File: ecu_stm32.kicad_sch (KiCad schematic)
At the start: 46 parts, among them J17 ARM Cortex Debug, Y2 16MHz

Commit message: Lots of routing
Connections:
- net +3.3V: now also R104.2
- net +3V3: no longer R104.2
- net IMU_INT1: now also U40.151 (PD7); no longer U40.152 (PG9)
- net IMU_INT2: now also U40.152 (PG9); no longer U40.151 (PD7)
- net RADIO1_DIO0: now also U40.19 (PF3); no longer U40.18 (PF2)
- net RADIO1_DIO1: now also U40.18 (PF2); no longer U40.19 (PF3)
- net RADIO2_DIO0: now also U40.12 (PI10); no longer U40.11 (PI9)
- net RADIO2_DIO1: now also U40.11 (PI9); no longer U40.12 (PI10)
- net RADIO_DIO0: now also U40.17 (PF1); no longer U40.16 (PF0)
- net RADIO_DIO1: now also U40.16 (PF0); no longer U40.17 (PF1)
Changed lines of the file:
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@@
 	(global_label "RADIO1_DIO1"
 		(shape input)
-		(at 193.04 76.2 0)
+		(at 193.04 73.66 0)
 		(fields_autoplaced yes)
 		(effects
@@
 		)
 		(property "Intersheetrefs" "${INTERSHEET_REFS}"
-			(at 208.181 76.2 0)
+			(at 208.181 73.66 0)
 			(effects
 				(font
@@
 	(global_label "RADIO2_DIO1"
 		(shape input)
-		(at 256.54 114.3 0)
+		(at 256.54 111.76 0)
 		(fields_autoplaced yes)
 		(effects
@@
 		)
 		(property "Intersheetrefs" "${INTERSHEET_REFS}"
-			(at 271.681 114.3 0)
+			(at 271.681 111.76 0)
 			(effects
 				(font
@@
 	(global_label "IMU_INT2"
 		(shape input)
-		(at 256.54 38.1 0)
+		(at 226.06 91.44 180)
 		(fields_autoplaced yes)
 		(effects
@@
 				(size 1.27 1.27)
 			)
-			(justify left)
+			(justify right)
 		)
 		(property "Intersheetrefs" "${INTERSHEET_REFS}"
-			(at 267.9919 38.1 0)
+			(at 214.6081 91.44 0)
 			(effects
 				(font
 					(size 1.27 1.27)
 				)
-				(justify left)
+				(justify right)
 				(hide yes)
 			)
@@
 	(global_label "RADIO_DIO0"
 		(shape input)
-		(at 193.04 68.58 0)
+		(at 193.04 71.12 0)
 		(fields_autoplaced yes)
 		(effects
@@
 		)
 		(property "Intersheetrefs" "${INTERSHEET_REFS}"
-			(at 206.9715 68.58 0)
+			(at 206.9715 71.12 0)
 			(effects
 				(font
@@
 	(global_label "RADIO2_DIO0"
 		(shape input)
-		(at 256.54 111.76 0)
+		(at 256.54 114.3 0)
 		(fields_autoplaced yes)
 		(effects
@@
 		)
 		(property "Intersheetrefs" "${INTERSHEET_REFS}"
-			(at 271.681 111.76 0)
+			(at 271.681 114.3 0)
 			(effects
 				(font
@@
 	(global_label "RADIO1_DIO0"
 		(shape input)
-		(at 193.04 73.66 0)
+		(at 193.04 76.2 0)
 		(fields_autoplaced yes)
 		(effects
@@
 		)
 		(property "Intersheetrefs" "${INTERSHEET_REFS}"
-			(at 208.181 73.66 0)
+			(at 208.181 76.2 0)
 			(effects
 				(font
@@
 	(global_label "IMU_INT1"
 		(shape input)
-		(at 226.06 91.44 180)
+		(at 256.54 38.1 0)
 		(fields_autoplaced yes)
 		(effects
@@
 				(size 1.27 1.27)
 			)
-			(justify right)
+			(justify left)
 		)
 		(property "Intersheetrefs" "${INTERSHEET_REFS}"
-			(at 214.6875 91.44 0)
+			(at 267.9919 38.1 0)
 			(effects
 				(font
 					(size 1.27 1.27)
 				)
-				(justify right)
+				(justify left)
 				(hide yes)
 			)
@@
 	(global_label "RADIO_DIO1"
 		(shape input)
-		(at 193.04 71.12 0)
+		(at 193.04 68.58 0)
 		(fields_autoplaced yes)
 		(effects
@@
 		)
 		(property "Intersheetrefs" "${INTERSHEET_REFS}"
-			(at 206.9715 71.12 0)
+			(at 206.9715 68.58 0)
 			(effects
 				(font
@@
 	)
 	(symbol
+		(lib_id "power:+3.3V")
+		(at 69.85 67.31 270)
+		(unit 1)
+		(exclude_from_sim no)
+		(in_bom yes)
+		(on_board yes)
+		(dnp no)
+		(property "Reference" "#PWR0228"
+			(at 66.04 67.31 0)
+			(effects
+				(font
+					(size 1.27 1.27)
+				)
+				(hide yes)
+			)
+		)
+		(property "Value" "+3.3V"
+			(at 73.66 67.31 0)
+			(effects
+				(font
+					(size 1.27 1.27)
+				)
+			)
+		)
+		(property "Footprint" ""
+			(at 69.85 67.31 0)
+			(effects
+				(font
+					(size 1.27 1.27)
+				)
+				(hide yes)
+			)
+		)
+		(property "Datasheet" ""
+			(at 69.85 67.31 0)
+			(effects
+				(font
+					(size 1.27 1.27)
+				)
+				(hide yes)
+			)
+		)
+		(property "Description" ""
+			(at 69.85 67.31 0)
+			(effects
+				(font
+					(size 1.27 1.27)
+				)
+				(hide yes)
+			)
+		)
+		(pin "1"
+		)
+		(instances
+			(project "rocket2-ecu"
+				(path "/02606b2c-b376-4ffb-9781-f9cea3f70994/d71af74c-6b83-4356-8066-aa44d85885b6"
+					(reference "#PWR0228")
+					(unit 1)
+				)
+			)
+		)
+	)
+	(symbol
 		(lib_id "Device:C_Small")
 		(at 80.01 129.54 90)
@@
 					(unit 1)
 				)
-			)
-		)
-	)
-	(symbol
-		(lib_id "power:+3V3")
-		(at 69.85 67.31 270)
-		(unit 1)
-		(exclude_from_sim no)
-		(in_bom yes)
-		(on_board yes)
-		(dnp no)
-		(property "Reference" "#PWR0228"
-			(at 66.04 67.31 0)
-			(effects
-				(font
-					(size 1.27 1.27)
-				)
-				(hide yes)
-			)
-		)
-		(property "Value" "+3V3"
-			(at 75.438 67.31 90)
-			(effects
-				(font
-					(size 1.27 1.27)
-				)
-			)
-		)
-		(property "Footprint" ""
-			(at 69.85 67.31 0)
-			(effects
-				(font
-					(size 1.27 1.27)
-				)
-				(hide yes)
-			)
-		)
-		(property "Datasheet" ""
-			(at 69.85 67.31 0)
-			(effects
-				(font
-					(size 1.27 1.27)
-				)
-				(hide yes)
-			)
-		)
-		(property "Description" ""
-			(at 69.85 67.31 0)
-			(effects
-				(font
-					(size 1.27 1.27)
-				)
-				(hide yes)
-			)
-		)
-		(pin "1"
-		)
-		(instances
-			(project "rocket2-ecu"
-				(path "/02606b2c-b376-4ffb-9781-f9cea3f70994/d71af74c-6b83-4356-8066-aa44d85885b6"
-					(reference "#PWR0228")
-					(unit 1)
-				)

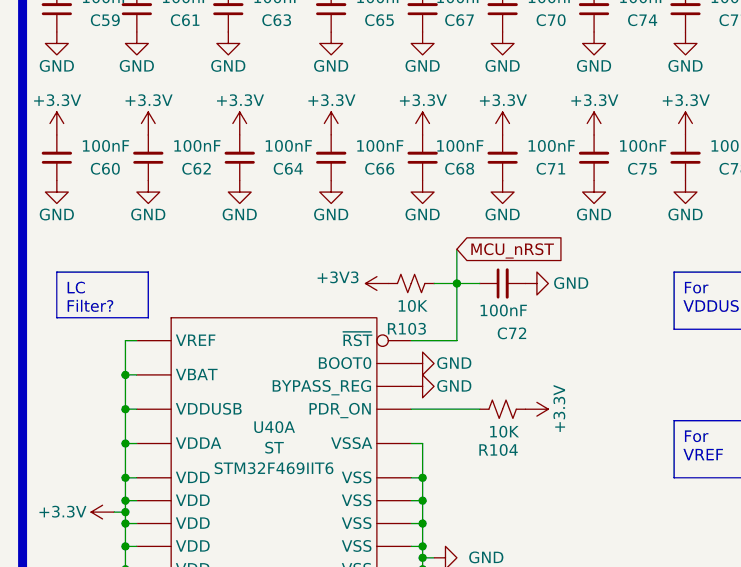
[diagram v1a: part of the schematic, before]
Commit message: More routing, only GPS and REDS radio left
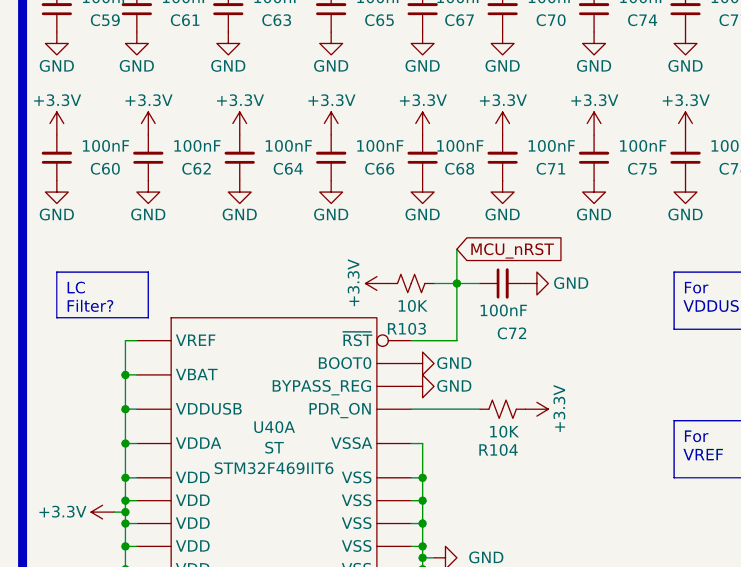
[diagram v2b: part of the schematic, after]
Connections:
- net +3V3 is gone; now on net +3.3V: R103.1
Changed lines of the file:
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@@
+	)
+	(symbol
+		(lib_id "power:+3.3V")
+		(at 54.61 53.34 90)
+		(unit 1)
+		(exclude_from_sim no)
+		(in_bom yes)
+		(on_board yes)
+		(dnp no)
+		(property "Reference" "#PWR075"
+			(at 58.42 53.34 0)
+			(effects
+				(font
+					(size 1.27 1.27)
+				)
+				(hide yes)
+			)
+		)
+		(property "Value" "+3.3V"
+			(at 50.8 53.34 0)
+			(effects
+				(font
+					(size 1.27 1.27)
+				)
+			)
+		)
+		(property "Footprint" ""
+			(at 54.61 53.34 0)
+			(effects
+				(font
+					(size 1.27 1.27)
+				)
+				(hide yes)
+			)
+		)
+		(property "Datasheet" ""
+			(at 54.61 53.34 0)
+			(effects
+				(font
+					(size 1.27 1.27)
+				)
+				(hide yes)
+			)
+		)
+		(property "Description" ""
+			(at 54.61 53.34 0)
+			(effects
+				(font
+					(size 1.27 1.27)
+				)
+				(hide yes)
+			)
+		)
+		(pin "1"
+		)
+		(instances
+			(project "rocket2-ecu"
+				(path "/02606b2c-b376-4ffb-9781-f9cea3f70994/d71af74c-6b83-4356-8066-aa44d85885b6"
+					(reference "#PWR075")
+					(unit 1)
+				)
+			)
+		)
 	)
 	(symbol
@@
 					(unit 1)
 				)
-			)
-		)
-	)
-	(symbol
-		(lib_id "power:+3V3")
-		(at 54.61 53.34 90)
-		(unit 1)
-		(exclude_from_sim no)
-		(in_bom yes)
-		(on_board yes)
-		(dnp no)
-		(fields_autoplaced yes)
-		(property "Reference" "#PWR0214"
-			(at 58.42 53.34 0)
-			(effects
-				(font
-					(size 1.27 1.27)
-				)
-				(hide yes)
-			)
-		)
-		(property "Value" "+3V3"
-			(at 51.435 52.705 90)
-			(effects
-				(font
-					(size 1.27 1.27)
-				)
-				(justify left)
-			)
-		)
-		(property "Footprint" ""
-			(at 54.61 53.34 0)
-			(effects
-				(font
-					(size 1.27 1.27)
-				)
-				(hide yes)
-			)
-		)
-		(property "Datasheet" ""
-			(at 54.61 53.34 0)
-			(effects
-				(font
-					(size 1.27 1.27)
-				)
-				(hide yes)
-			)
-		)
-		(property "Description" ""
-			(at 54.61 53.34 0)
-			(effects
-				(font
-					(size 1.27 1.27)
-				)
-				(hide yes)
-			)
-		)
-		(pin "1"
-		)
-		(instances
-			(project "rocket2-ecu"
-				(path "/02606b2c-b376-4ffb-9781-f9cea3f70994/d71af74c-6b83-4356-8066-aa44d85885b6"
-					(reference "#PWR0214")
-					(unit 1)
-				)

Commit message: Updated with Daniels suggestions
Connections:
- net ETH_RX: now also U40.79 (PB10); no longer U40.80 (PB11)
- net ETH_TX: now also U40.80 (PB11); no longer U40.79 (PB10)
- net GPS_RX: now also U40.40 (PA0); no longer U40.41 (PA1)
- net GPS_TX: now also U40.41 (PA1); no longer U40.40 (PA0)
- net GPS_SCL: no longer names the net of U40.45 (PH4)
- net GPS_SDA: no longer names the net of U40.46 (PH5)
- no-connect marks 71 -> 73
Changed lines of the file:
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@@
 	)
 	(no_connect
+		(at 256.54 78.74)
+	)
+	(no_connect
+		(at 256.54 81.28)
+	)
+	(no_connect
 		(at 256.54 40.64)
 	)
@@
 	(global_label "GPS_RX"
 		(shape input)
-		(at 162.56 22.86 180)
+		(at 162.56 20.32 180)
 		(fields_autoplaced yes)
 		(effects
@@
 		)
 		(property "Intersheetrefs" "${INTERSHEET_REFS}"
-			(at 152.3782 22.86 0)
+			(at 152.3782 20.32 0)
 			(effects
 				(font
@@
 		)
 	)
-	(global_label "GPS_SCL"
-		(shape input)
-		(at 256.54 78.74 0)
-		(fields_autoplaced yes)
-		(effects
-			(font
-				(size 1.27 1.27)
-			)
-			(justify left)
-		)
-		(property "Intersheetrefs" "${INTERSHEET_REFS}"
-			(at 267.6705 78.74 0)
-			(effects
-				(font
-					(size 1.27 1.27)
-				)
-				(justify left)
-				(hide yes)
-			)
-		)
-	)
 	(global_label "MCU_nRST"
 		(shape input)
@@
 	(global_label "ETH_TX"
 		(shape input)
-		(at 193.04 45.72 0)
-		(fields_autoplaced yes)
-		(effects
-			(font
-				(size 1.27 1.27)
-			)
-			(justify left)
-		)
-		(property "Intersheetrefs" "${INTERSHEET_REFS}"
-			(at 202.5376 45.72 0)
-			(effects
-				(font
-					(size 1.27 1.27)
-				)
-				(justify left)
-				(hide yes)
-			)
-		)
-	)
-	(global_label "GPS_SDA"
-		(shape input)
-		(at 256.54 81.28 0)
+		(at 193.04 48.26 0)
 		(fields_autoplaced yes)
 		(effects
@@
 		)
 		(property "Intersheetrefs" "${INTERSHEET_REFS}"
-			(at 267.731 81.28 0)
+			(at 202.5376 48.26 0)
 			(effects
 				(font
@@
 	(global_label "ETH_RX"
 		(shape input)
-		(at 193.04 48.26 0)
+		(at 193.04 45.72 0)
 		(fields_autoplaced yes)
 		(effects
@@
 		)
 		(property "Intersheetrefs" "${INTERSHEET_REFS}"
-			(at 202.84 48.26 0)
+			(at 202.84 45.72 0)
 			(effects
 				(font
@@
 	(global_label "GPS_TX"
 		(shape input)
-		(at 162.56 20.32 180)
+		(at 162.56 22.86 180)
 		(fields_autoplaced yes)
 		(effects
@@
 		)
 		(property "Intersheetrefs" "${INTERSHEET_REFS}"
-			(at 152.6806 20.32 0)
+			(at 152.6806 22.86 0)
 			(effects
 				(font

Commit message: new BOM
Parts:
- C59, C60, C61, C62, C63, C64, C65, C66, C67, C68, C70, C71, C72, C74, C75, C77, C78, C79, C80, C81, C82, C83, C84, C88, C89: Part # Generic 100nF 6.3V X7R 0402 MLCC -> Generic CAP CER 0.1UF 6.3V X7R 0402
- C69, C73, C90: Part # Generic 0603 2.2uF 6.3V X7R MLCC -> Generic CAP CER 2.2UF 6.3V X7R 0603
- C76: Part # Generic 0603 10uF 6.3V X7R MLCC -> Generic CAP CER 10UF 50V X7R 0603
- C85, C87: Part # Generic 0603 1uF 6.3V X7R MLCC -> Generic CAP CER 1UF 50V X7R 0603
- C86: Part # Generic 0603 4.7uF 6.3V X7R MLCC -> Generic CAP CER 4.7UF 6.3V X7R 0603
- D34, D35: value ESD321 -> 6.8V; Manufacturer TI -> Texas Instruments
- J16: value ~ -> USB-C
- R103, R104, R107, R108: Part # Generic 10K 1% 0402 Resistor -> Generic RES SMD 10K OHM 1% 1/4W 0402
- R105, R106: Part # Generic 0603 5.1K 1% Resistor -> Generic RES SMD 5.1K OHM 1% 1/16W 0402
- R109: value 100R -> 100; Part # Generic 100R 1% 0402 Resistor -> Generic RES SMD 100 OHM 1% 1/4W 0402
- U40: Manufacturer ST -> STMicroelectronics
- Y2: Manufacturer ECS -> ECS Inc.
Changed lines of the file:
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@@
 			)
 		)
-		(property "Value" "~"
+		(property "Value" "USB-C"
 			(at 57.15 147.32 0)
 			(effects
@@
 			)
 		)
-		(property "Part #" "Generic 100nF 6.3V X7R 0402 MLCC"
+		(property "Part #" "Generic CAP CER 0.1UF 6.3V X7R 0402"
 			(at 97.79 22.86 0)
 			(effects
@@
 			)
 		)
-		(property "Part #" "Generic 100nF 6.3V X7R 0402 MLCC"
+		(property "Part #" "Generic CAP CER 0.1UF 6.3V X7R 0402"
 			(at 87.63 22.86 0)
 			(effects
@@
 			)
 		)
-		(property "Manufacturer" "ECS"
+		(property "Manufacturer" "ECS Inc."
 			(at 271.78 64.77 0)
 			(effects
@@
 			)
 		)
-		(property "Part #" "Generic 10K 1% 0402 Resistor"
+		(property "Part #" "Generic RES SMD 10K OHM 1% 1/4W 0402"
 			(at 57.15 53.34 0)
 			(effects
@@
 			)
 		)
-		(property "Part #" "Generic 100nF 6.3V X7R 0402 MLCC"
+		(property "Part #" "Generic CAP CER 0.1UF 6.3V X7R 0402"
 			(at 26.67 22.86 0)
 			(effects
@@
 			)
 		)
-		(property "Part #" "Generic 0603 5.1K 1% Resistor"
+		(property "Part #" "Generic RES SMD 5.1K OHM 1% 1/16W 0402"
 			(at 77.47 147.32 0)
 			(effects
@@
 			)
 		)
-		(property "Part #" "Generic 0603 10uF 6.3V X7R MLCC"
+		(property "Part #" "Generic CAP CER 10UF 50V X7R 0603"
 			(at 80.01 129.54 0)
 			(effects
@@
 			)
 		)
-		(property "Value" "ESD321"
+		(property "Value" "6.8V"
 			(at 35.56 140.97 90)
 			(effects
@@
 			)
 		)
-		(property "Datasheet" "~"
+		(property "Datasheet" "https://www.ti.com/general/docs/suppproductinfo.tsp?distId=10&gotoUrl=https%3A%2F%2Fwww.ti.com%2Flit%2Fgpn%2Fesd321"
 			(at 39.37 144.78 90)
 			(effects
@@
 			)
 		)
-		(property "Manufacturer" "TI"
+		(property "Manufacturer" "Texas Instruments"
 			(at 39.37 144.78 0)
 			(effects
@@
 			)
 		)
-		(property "Part #" "Generic 100nF 6.3V X7R 0402 MLCC"
+		(property "Part #" "Generic CAP CER 0.1UF 6.3V X7R 0402"
 			(at 27.94 39.37 0)
 			(effects
@@
 			)
 		)
-		(property "Part #" "Generic 100nF 6.3V X7R 0402 MLCC"
+		(property "Part #" "Generic CAP CER 0.1UF 6.3V X7R 0402"
 			(at 58.42 39.37 0)
 			(effects
@@
 			)
 		)
-		(property "Part #" "Generic 0603 2.2uF 6.3V X7R MLCC"
+		(property "Part #" "Generic CAP CER 2.2UF 6.3V X7R 0603"
 			(at 60.96 109.22 0)
 			(effects
@@
 			)
 		)
-		(property "Part #" "Generic 100nF 6.3V X7R 0402 MLCC"
+		(property "Part #" "Generic CAP CER 0.1UF 6.3V X7R 0402"
 			(at 109.22 39.37 0)
 			(effects
@@
 			)
 		)
-		(property "Part #" "Generic 0603 2.2uF 6.3V X7R MLCC"
+		(property "Part #" "Generic CAP CER 2.2UF 6.3V X7R 0603"
 			(at 198.12 123.19 0)
 			(effects
@@
 			)
 		)
-		(property "Part #" "Generic 100nF 6.3V X7R 0402 MLCC"
+		(property "Part #" "Generic CAP CER 0.1UF 6.3V X7R 0402"
 			(at 17.78 39.37 0)
 			(effects
@@
 			)
 		)
-		(property "Manufacturer" "ST"
+		(property "Manufacturer" "STMicroelectronics"
 			(at 241.3 25.4 0)
 			(effects
@@
 			)
 		)
-		(property "Part #" "Generic 100nF 6.3V X7R 0402 MLCC"
+		(property "Part #" "Generic CAP CER 0.1UF 6.3V X7R 0402"
 			(at 87.63 39.37 0)
 			(effects
@@
 			)
 		)
-		(property "Part #" "Generic 100nF 6.3V X7R 0402 MLCC"
+		(property "Part #" "Generic CAP CER 0.1UF 6.3V X7R 0402"
 			(at 99.06 55.88 0)
 			(effects
@@
 			)
 		)
-		(property "Part #" "Generic 0603 4.7uF 6.3V X7R MLCC"
+		(property "Part #" "Generic CAP CER 4.7UF 6.3V X7R 0603"
 			(at 119.38 39.37 0)
 			(effects
@@
 			)
 		)
-		(property "Part #" "Generic 0603 5.1K 1% Resistor"
+		(property "Part #" "Generic RES SMD 5.1K OHM 1% 1/16W 0402"
 			(at 77.47 139.7 0)
 			(effects
@@
 			)
 		)
-		(property "Manufacturer" "ST"
+		(property "Manufacturer" "STMicroelectronics"
 			(at 41.91 71.628 0)
 			(effects
@@
 			)
 		)
-		(property "Part #" "Generic 100nF 6.3V X7R 0402 MLCC"
+		(property "Part #" "Generic CAP CER 0.1UF 6.3V X7R 0402"
 			(at 77.47 39.37 0)
 			(effects
@@
 			)
 		)
-		(property "Datasheet" ""
+		(property "Datasheet" "~"
 			(at 113.03 154.94 0)
 			(effects
@@
 			)
 		)
-		(property "Part #" "Generic 100nF 6.3V X7R 0402 MLCC"
+		(property "Part #" "Generic CAP CER 0.1UF 6.3V X7R 0402"
 			(at 36.83 22.86 0)
 			(effects
@@
 			)
 		)
-		(property "Manufacturer" "ST"
+		(property "Manufacturer" "STMicroelectronics"
 			(at 177.8 115.57 0)
 			(effects
@@
 			)
 		)
-		(property "Part #" "Generic 0603 2.2uF 6.3V X7R MLCC"
+		(property "Part #" "Generic CAP CER 2.2UF 6.3V X7R 0603"
 			(at 69.85 109.22 0)
 			(effects
@@
 			)
 		)
-		(property "Part #" "Generic 0603 1uF 6.3V X7R MLCC"
+		(property "Part #" "Generic CAP CER 1UF 50V X7R 0603"
 			(at 120.65 55.88 0)
 			(effects
@@
 			)
 		)
-		(property "Part #" "Generic 100nF 6.3V X7R 0402 MLCC"
+		(property "Part #" "Generic CAP CER 0.1UF 6.3V X7R 0402"
 			(at 38.1 39.37 0)
 			(effects
@@
 			)
 		)
-		(property "Value" "ESD321"
+		(property "Value" "6.8V"
 			(at 25.4 146.05 90)
 			(effects
@@
 			)
 		)
-		(property "Datasheet" "~"
+		(property "Datasheet" "https://www.ti.com/general/docs/suppproductinfo.tsp?distId=10&gotoUrl=https%3A%2F%2Fwww.ti.com%2Flit%2Fgpn%2Fesd321"
 			(at 34.29 144.78 90)
 			(effects
@@
 			)
 		)
-		(property "Manufacturer" "TI"
+		(property "Manufacturer" "Texas Instruments"
 			(at 34.29 144.78 0)
 			(effects
@@
 			)
 		)
-		(property "Manufacturer" "ST"
+		(property "Manufacturer" "STMicroelectronics"
 			(at 241.3 78.74 0)
 			(effects
@@
 			)
 		)
-		(property "Part #" "Generic 10K 1% 0402 Resistor"
+		(property "Part #" "Generic RES SMD 10K OHM 1% 1/4W 0402"
 			(at 67.31 67.31 0)
 			(effects
@@
 			)
 		)
-		(property "Part #" "Generic 100nF 6.3V X7R 0402 MLCC"
+		(property "Part #" "Generic CAP CER 0.1UF 6.3V X7R 0402"
 			(at 67.31 22.86 0)
 			(effects
@@
 			)
 		)
-		(property "Value" "100R"
+		(property "Value" "100"
 			(at 220.726 144.78 0)
 			(effects
@@
 			)
 		)
-		(property "Part #" "Generic 100R 1% 0402 Resistor"
+		(property "Part #" "Generic RES SMD 100 OHM 1% 1/4W 0402"
 			(at 215.9 143.51 0)
 			(effects
@@
 			)
 		)
-		(property "Part #" "Generic 100nF 6.3V X7R 0402 MLCC"
+		(property "Part #" "Generic CAP CER 0.1UF 6.3V X7R 0402"
 			(at 17.78 22.86 0)
 			(effects
@@
 			)
 		)
-		(property "Part #" "Generic 100nF 6.3V X7R 0402 MLCC"
+		(property "Part #" "Generic CAP CER 0.1UF 6.3V X7R 0402"
 			(at 97.79 39.37 0)
 			(effects
@@
 			)
 		)
-		(property "Manufacturer" "ST"
+		(property "Manufacturer" "STMicroelectronics"
 			(at 177.8 73.66 0)
 			(effects
@@
 			)
 		)
-		(property "Part #" "Generic 100nF 6.3V X7R 0402 MLCC"
+		(property "Part #" "Generic CAP CER 0.1UF 6.3V X7R 0402"
 			(at 48.26 39.37 0)
 			(effects
@@
 			)
 		)
-		(property "Part #" "Generic 100nF 6.3V X7R 0402 MLCC"
+		(property "Part #" "Generic CAP CER 0.1UF 6.3V X7R 0402"
 			(at 67.31 39.37 0)
 			(effects
@@
 			)
 		)
-		(property "Part #" "Generic 100nF 6.3V X7R 0402 MLCC"
+		(property "Part #" "Generic CAP CER 0.1UF 6.3V X7R 0402"
 			(at 130.81 73.66 0)
 			(effects
@@
 			)
 		)
-		(property "Part #" "Generic 100nF 6.3V X7R 0402 MLCC"
+		(property "Part #" "Generic CAP CER 0.1UF 6.3V X7R 0402"
 			(at 58.42 22.86 0)
 			(effects
@@
 			)
 		)
-		(property "Part #" "Generic 100nF 6.3V X7R 0402 MLCC"
+		(property "Part #" "Generic CAP CER 0.1UF 6.3V X7R 0402"
 			(at 130.81 55.88 0)
 			(effects
@@
 			)
 		)
-		(property "Part #" "Generic 100nF 6.3V X7R 0402 MLCC"
+		(property "Part #" "Generic CAP CER 0.1UF 6.3V X7R 0402"
 			(at 107.95 22.86 0)
 			(effects
@@
 			)
 		)
-		(property "Part #" "Generic 10K 1% 0402 Resistor"
+		(property "Part #" "Generic RES SMD 10K OHM 1% 1/4W 0402"
 			(at 111.76 132.08 0)
 			(effects
@@
 			)
 		)
-		(property "Manufacturer" "ST"
+		(property "Manufacturer" "STMicroelectronics"
 			(at 177.8 25.4 0)
 			(effects
@@
 			)
 		)
-		(property "Part #" "Generic 100nF 6.3V X7R 0402 MLCC"
+		(property "Part #" "Generic CAP CER 0.1UF 6.3V X7R 0402"
 			(at 99.06 72.39 0)
 			(effects
@@
 			)
 		)
-		(property "Part #" "Generic 100nF 6.3V X7R 0402 MLCC"
+		(property "Part #" "Generic CAP CER 0.1UF 6.3V X7R 0402"
 			(at 48.26 22.86 0)
 			(effects
@@
 			)
 		)
-		(property "Part #" "Generic 10K 1% 0402 Resistor"
+		(property "Part #" "Generic RES SMD 10K OHM 1% 1/4W 0402"
 			(at 121.92 132.08 0)
 			(effects
@@
 			)
 		)
-		(property "Part #" "Generic 0603 1uF 6.3V X7R MLCC"
+		(property "Part #" "Generic CAP CER 1UF 50V X7R 0603"
 			(at 109.22 72.39 0)
 			(effects
@@
 			)
 		)
-		(property "Part #" "Generic 100nF 6.3V X7R 0402 MLCC"
+		(property "Part #" "Generic CAP CER 0.1UF 6.3V X7R 0402"
 			(at 67.31 53.34 0)
 			(effects
@@
 			)
 		)
-		(property "Part #" "Generic 100nF 6.3V X7R 0402 MLCC"
+		(property "Part #" "Generic CAP CER 0.1UF 6.3V X7R 0402"
 			(at 77.47 22.86 0)
 			(effects
